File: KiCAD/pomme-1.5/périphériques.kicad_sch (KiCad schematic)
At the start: 10 parts, among them Q1 2N3906, Q2 2N3904

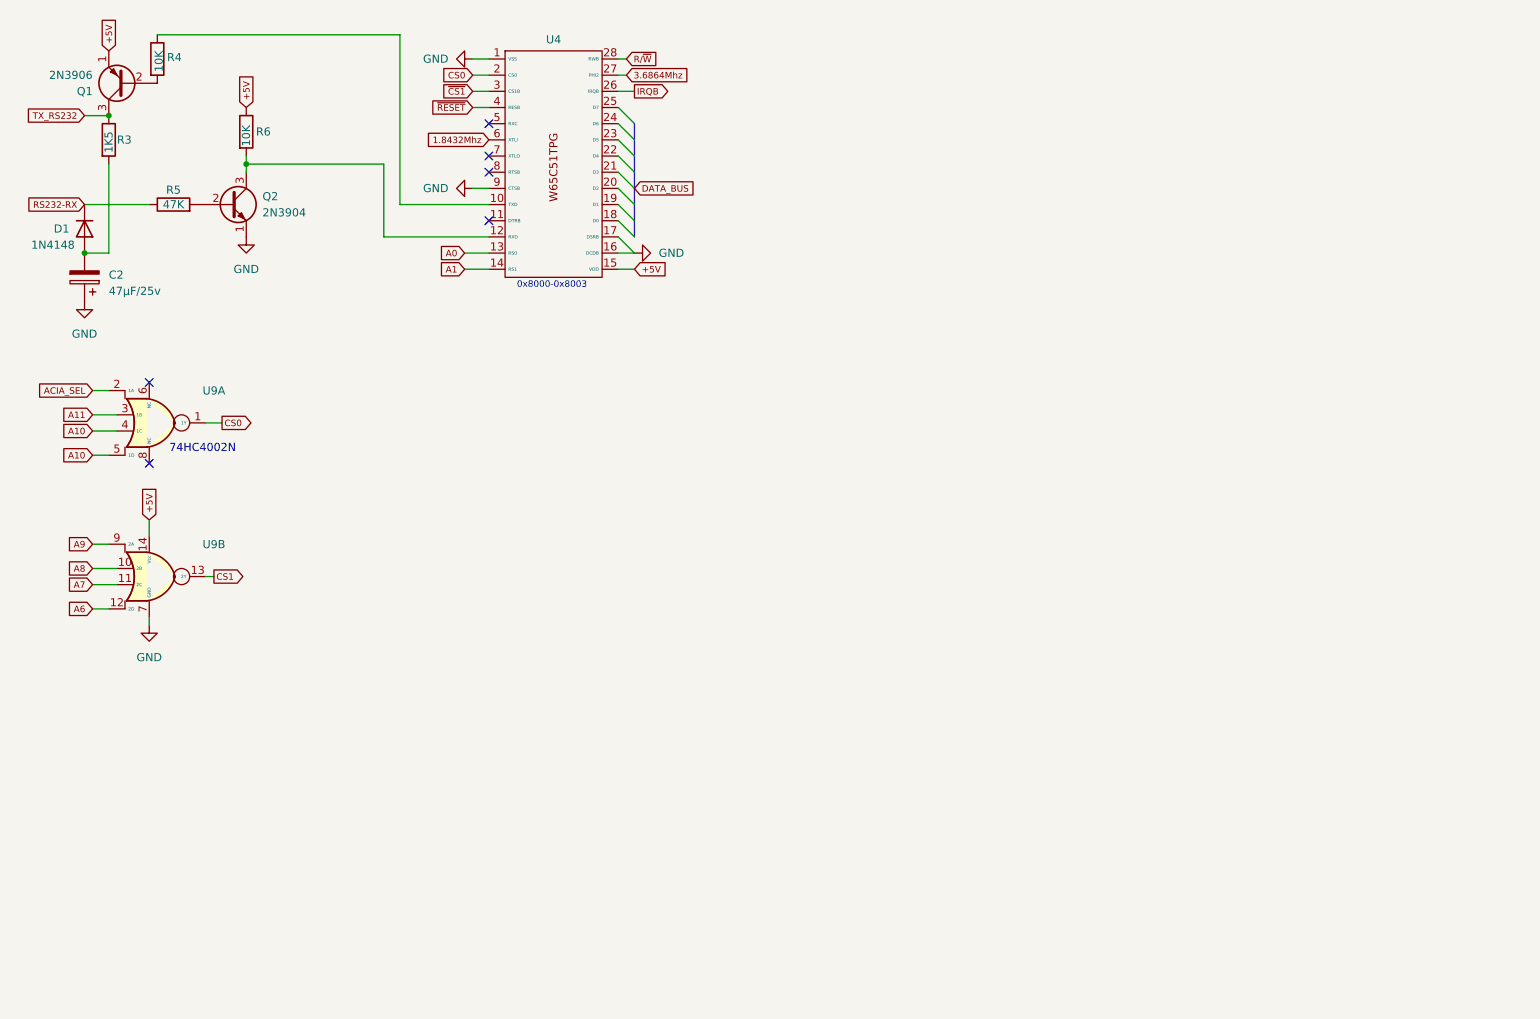
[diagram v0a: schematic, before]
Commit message: Modification de test1.s et de la schématique. L'ordinateur fonctionne à 3.68Mhz
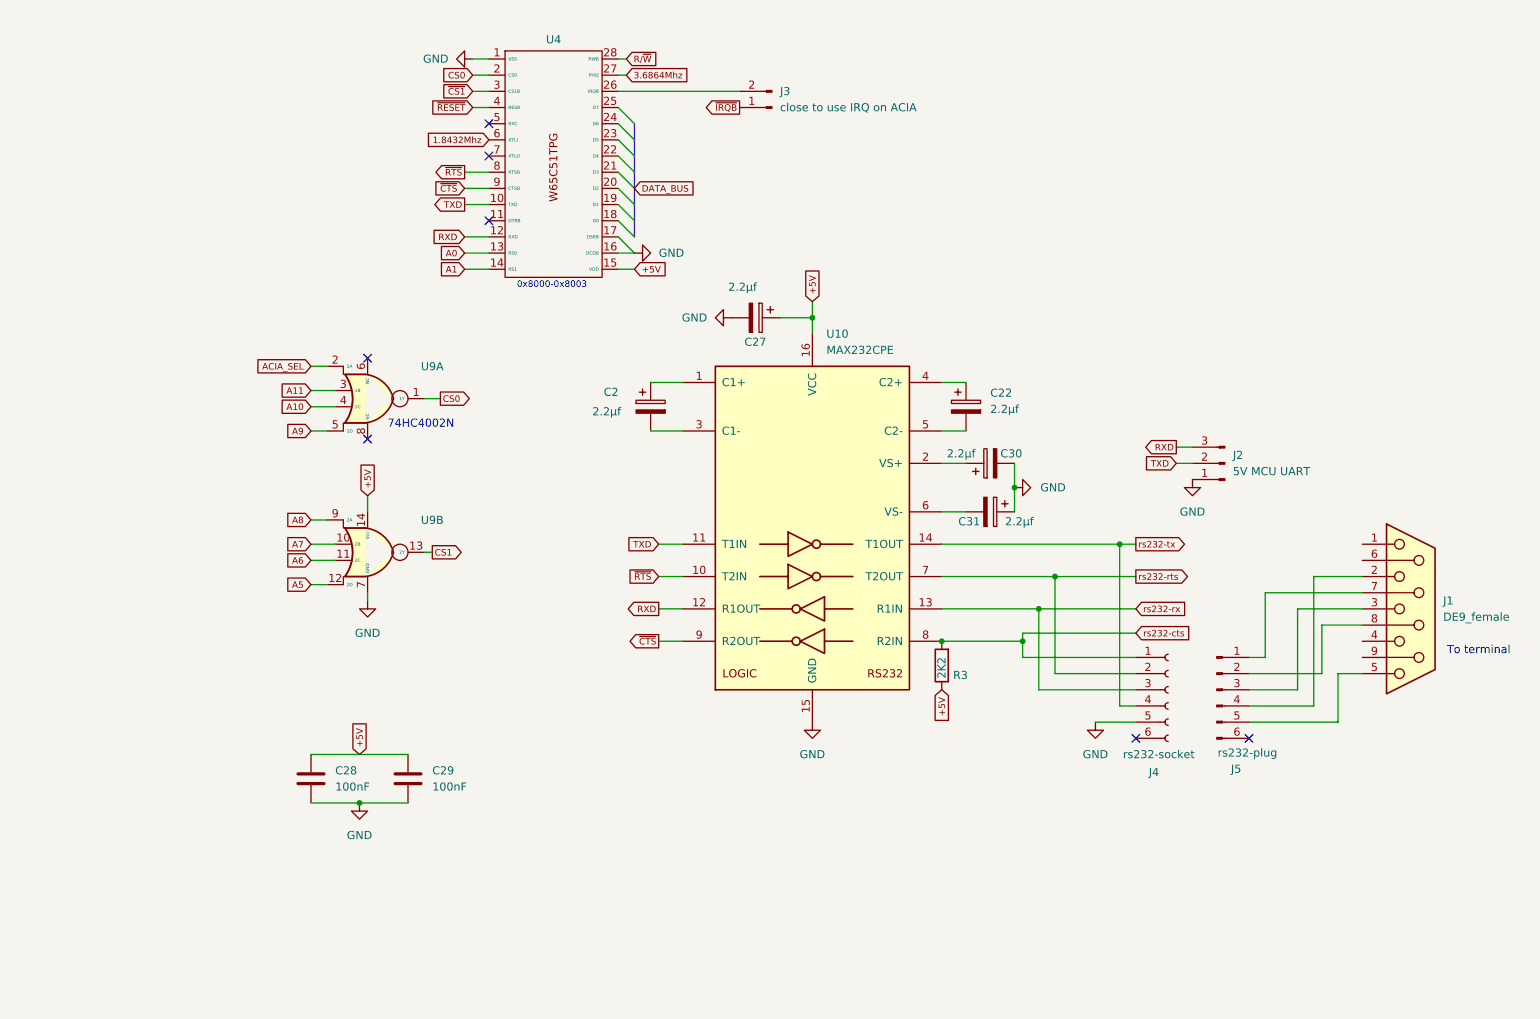
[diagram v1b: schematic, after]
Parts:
- removed D1: 1N4148, Diode_THT:D_DO-35_SOD27_P7.62mm_Horizontal, symbol Diode:1N4148
- removed Q1: 2N3906, Package_TO_SOT_THT:TO-92_Inline, symbol Transistor_BJT:2N3906
- removed Q2: 2N3904, Package_TO_SOT_THT:TO-92_Inline, symbol Transistor_BJT:2N3904
- removed R4, R6: 10K, symbol Device:R
- removed R5: 47K, symbol Device:R
- added C22, C27, C30, C31: 2.2µf, symbol Device:C_Polarized
- added C28, C29: 100nF, symbol Device:C
- added J1: DE9_female, symbol Connector:DE9_Receptacle
- added J2: 5V MCU UART, symbol Connector:Conn_01x03_Pin
- added J3: close to use IRQ on ACIA, symbol Connector:Conn_01x02_Pin
- added J4: rs232-socket, symbol Connector:Conn_01x06_Socket
- added J5: rs232-plug, symbol Connector:Conn_01x06_Pin
- added U10: MAX232CPE, symbol Interface_UART:MAX232
- C2: value 47µF/25v -> 2.2µf
- R3: value 1K5 -> 2K2
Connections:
- net TX_RS232 is gone; now on net +5V: R3.1
- net +5V: now also C27.1, C28.2, C29.1, U10.16 (VCC)
- net A10: no longer U9.5 (1D)
- net A6: now also U9.11 (2C); no longer U9.12 (2D)
- net A7: now also U9.10 (2B); no longer U9.11 (2C)
- net A8: now also U9.9 (2A); no longer U9.10 (2B)
- net A9: now also U9.5 (1D); no longer U9.9 (2A)
- net GND: now also C27.2, C28.1, C29.2, C30.2, C31.1, J2.1 (Pin_1), J4.5 (Pin_5), U10.15 (GND); no longer C2.1, U4.9 (CTSB)
- net at C2.2: now also U10.3 (C1-); no longer R3.2
- net RXD: now reaches U4.12 (RXD)
- net RXD: now also J2.3 (Pin_3), U10.12 (R1OUT)
- net TXD: now reaches U4.10 (TXD)
- net TXD: now also J2.2 (Pin_2), U10.11 (T1IN)
- net ~{RTS}: now reaches U4.8 (RTSB)
- net ~{RTS}: now also U10.10 (T2IN)
- net IRQB: no longer names the net of U4.26 (IRQB)
- net IRQB: now also J3.2 (Pin_2)
- new net: C22.1, U10.4 (C2+)
- new net: C22.2, U10.5 (C2-)
- new net: C30.1, U10.2 (VS+)
- new net: C2.1, U10.1 (C1+)
- new net: C31.2, U10.6 (VS-)
- new net: J1.2, J5.4 (Pin_4)
- new net: J1.3, J5.3 (Pin_3)
- new net: J1.5, J5.5 (Pin_5)
- new net: J1.7, J5.1 (Pin_1)
- new net: J1.8, J5.2 (Pin_2)
- new net A5: U9.12 (2D)
- new net rs232-cts: J4.1 (Pin_1), R3.2, U10.8 (R2IN)
- new net rs232-rts: J4.2 (Pin_2), U10.7 (T2OUT)
- new net rs232-rx: J4.3 (Pin_3), U10.13 (R1IN)
- new net rs232-tx: J4.4 (Pin_4), U10.14 (T1OUT)
- new net ~{CTS}: U10.9 (R2OUT), U4.9 (CTSB)
- new net ~{IRQB}: J3.1 (Pin_1)
- no-connect marks 6 -> 7
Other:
- note added: "To terminal"
- moved on the sheet: U9A, U9B

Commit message: Ajout de p1+_terminal au projet
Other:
- note added: "0xD000-0xD003"
- note removed: "0x8000-0x8003"
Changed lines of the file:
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@@
 		)
 	)
-	(text "0x8000-0x8003"
+	(text "0xD000-0xD003"
 		(exclude_from_sim no)
 		(at 131.826 67.31 0)

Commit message: Remplacement du p1+ drive par un circuit différent et modication à p1+ terminal et au pomme 1+
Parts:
- added Q3: 2N3904, Package_TO_SOT_THT:TO-92_Inline, symbol Transistor_BJT:2N3904
- added R16: 3K9, symbol Device:R
- added R17: 10K, symbol Device:R
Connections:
- net +5V: now also R16.1, R17.1
- net RXD: no longer U10.12 (R1OUT), U4.12 (RXD)
- net ACIA_SEL renamed ~{p_select}
- new net: Q3.2 (B), R16.2
- new net: Q3.1 (E), U10.12 (R1OUT)
- new net ACIA RXD: Q3.3 (C), R17.2, U4.12 (RXD)
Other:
- note added: "ACIA serial communication adapter"
- note added: "NOTE: ACIA RXD shared use required open collector circuitry using 2N3904 on each device connected"
- note added: "see note near ACIA RXD"
- moved on the sheet: C28, C29
